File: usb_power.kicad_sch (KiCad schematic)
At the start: 38 parts, among them J1 USB_C_Receptacle_USB2.0_14P, Q1 IRLML6402, SW25 SW_Push_DPDT, U12 CH340N, U13 TP4056-42-ESOP8, U14 SX1308, U15 LM393

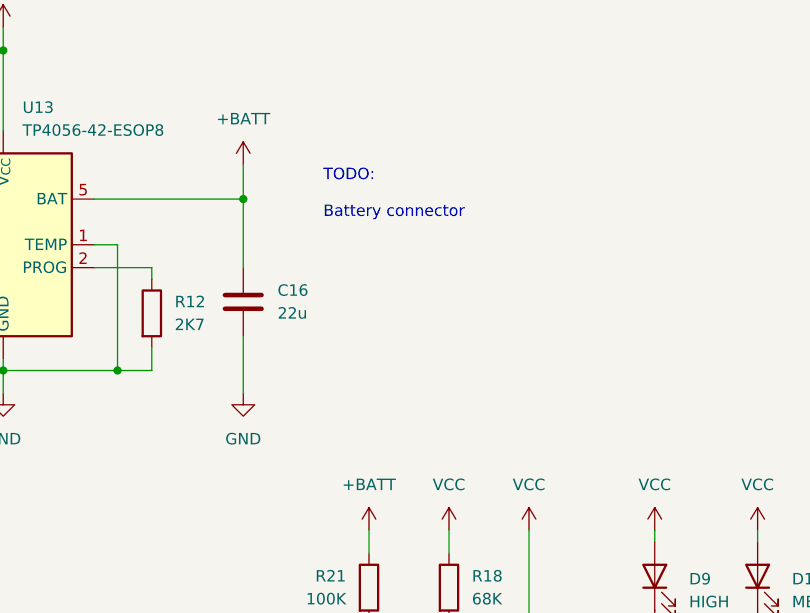
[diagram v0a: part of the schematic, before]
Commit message: HW: Add LiPo connector
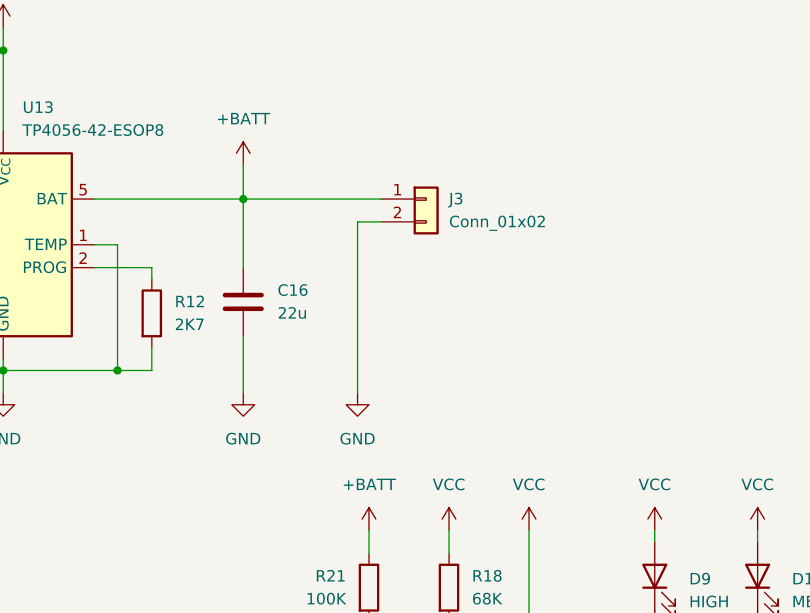
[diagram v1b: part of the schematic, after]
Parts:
- added J3: Conn_01x02, Connector_JST:JST_PH_B2B-PH-K_1x02_P2.00mm_Vertical, symbol Connector_Generic:Conn_01x02
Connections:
- net +BATT: now also J3.1 (Pin_1)
- net GND: now also J3.2 (Pin_2)
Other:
- note removed: "TODO: Battery connector"
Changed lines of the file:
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@@
 		(company "A.K.")
 	)
-	(text "TODO:\n\nBattery connector"
-		(exclude_from_sim no)
-		(at 203.2 47.752 0)
-		(effects
-			(font
-				(size 1.27 1.27)
-			)
-			(justify left)
-		)
-	)
 	(text_box "Voltage levels:\nHigh   >= 3.95 V\nMedium >= 3.28 V"
 		(exclude_from_sim no)
@@
 	(wire
 		(pts
+			(xy 207.01 69.85) (xy 207.01 50.8)
+		)
+		(stroke
+			(width 0)
+			(type default)
+		)
+	)
+	(wire
+		(pts
 			(xy 91.44 120.65) (xy 91.44 118.11)
 		)
@@
 	(wire
 		(pts
+			(xy 207.01 50.8) (xy 209.55 50.8)
+		)
+		(stroke
+			(width 0)
+			(type default)
+		)
+	)
+	(wire
+		(pts
 			(xy 123.19 135.89) (xy 123.19 137.16)
 		)
@@
 	(wire
 		(pts
+			(xy 194.31 48.26) (xy 209.55 48.26)
+		)
+		(stroke
+			(width 0)
+			(type default)
+		)
+	)
+	(wire
+		(pts
 			(xy 180.34 67.31) (xy 180.34 53.34)
 		)
@@
 	)
 	(symbol
+		(lib_id "Connector_Generic:Conn_01x02")
+		(at 214.63 48.26 0)
+		(unit 1)
+		(exclude_from_sim no)
+		(in_bom yes)
+		(on_board yes)
+		(dnp no)
+		(fields_autoplaced yes)
+		(property "Reference" "J3"
+			(at 217.17 48.2599 0)
+			(effects
+				(font
+					(size 1.27 1.27)
+				)
+				(justify left)
+			)
+		)
+		(property "Value" "Conn_01x02"
+			(at 217.17 50.7999 0)
+			(effects
+				(font
+					(size 1.27 1.27)
+				)
+				(justify left)
+			)
+		)
+		(property "Footprint" "Connector_JST:JST_PH_B2B-PH-K_1x02_P2.00mm_Vertical"
+			(at 214.63 48.26 0)
+			(effects
+				(font
+					(size 1.27 1.27)
+				)
+				(hide yes)
+			)
+		)
+		(property "Datasheet" "~"
+			(at 214.63 48.26 0)
+			(effects
+				(font
+					(size 1.27 1.27)
+				)
+				(hide yes)
+			)
+		)
+		(property "Description" "Generic connector, single row, 01x02, script generated (kicad-library-utils/schlib/autogen/connector/)"
+			(at 214.63 48.26 0)
+			(effects
+				(font
+					(size 1.27 1.27)
+				)
+				(hide yes)
+			)
+		)
+		(pin "2"
+		)
+		(pin "1"
+		)
+		(instances
+			(project ""
+				(path "/328c075d-c706-4d2d-bd37-a88a0c604482/c1e7a431-6e5f-4fa2-b435-dab397db0168"
+					(reference "J3")
+					(unit 1)
+				)
+			)
+		)
+	)
+	(symbol
 		(lib_id "Device:R")
 		(at 60.96 59.69 180)
@@
 					(unit 1)
 				)
+			)
+		)
+	)
+	(symbol
+		(lib_id "power:GND")
+		(at 207.01 69.85 0)
+		(unit 1)
+		(exclude_from_sim no)
+		(in_bom yes)
+		(on_board yes)
+		(dnp no)
+		(fields_autoplaced yes)
+		(property "Reference" "#PWR0143"
+			(at 207.01 76.2 0)
+			(effects
+				(font
+					(size 1.27 1.27)
+				)
+				(hide yes)
+			)
+		)
+		(property "Value" "GND"
+			(at 207.01 74.93 0)
+			(effects
+				(font
+					(size 1.27 1.27)
+				)
+			)
+		)
+		(property "Footprint" ""
+			(at 207.01 69.85 0)
+			(effects
+				(font
+					(size 1.27 1.27)
+				)
+				(hide yes)
+			)
+		)
+		(property "Datasheet" ""
+			(at 207.01 69.85 0)
+			(effects
+				(font
+					(size 1.27 1.27)
+				)
+				(hide yes)
+			)
+		)
+		(property "Description" "Power symbol creates a global label with name \"GND\" , ground"
+			(at 207.01 69.85 0)
+			(effects
+				(font
+					(size 1.27 1.27)
+				)
+				(hide yes)
+			)
+		)
+		(pin "1"
+		)
+		(instances
+			(project "pocket80"
+				(path "/328c075d-c706-4d2d-bd37-a88a0c604482/c1e7a431-6e5f-4fa2-b435-dab397db0168"
+					(reference "#PWR0143")
+					(unit 1)
+				)
